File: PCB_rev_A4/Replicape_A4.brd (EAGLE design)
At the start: 100 x 69.6 mm, 191 parts, among them P8 F-2X23-, P9 F-2X23-, Q1 AON6758, Q2 AON6758, Q3 AON6758, Q4 NIF5002, Q5 NIF5002, Q6 NIF5002, U1 SN74AHC595PW, U10 RT8268, U11 PCA9685PW, U12 DAC088S085, U13 DRV8825PWP, U14 DRV8825PWP, U15 DRV8825PWP, U16 DRV8825PWP, U17 DRV8825PWP, U18 CAT24C256, U2 SN74AHC595PW, U3 SN74AHC595PW, U4 SN74AHC595PW, U5 SN74AHC595PW, U6 MCP16321, U7 MCP1402, U8 MCP1402, U9 MCP1402, X1 22-05-7028-02, X10 22-05-7028-02, X11 22-05-7028-02, X12 22-05-7038-03, X13 22-05-7028-02, X14 22-05-7048-04, X15 22-05-7048-04, X16 22-05-7048-04, X17 22-05-7048-04, X18 22-05-7048-04, X19 22-05-7028-02, X2 MSTBA4, X20 MSTBA4, X21 MSTBA2, X23 22-05-7028-02, X3 MSTBA2, X4 22-05-7028-02, X5 22-05-7028-02, X6 22-05-7028-02, X7 22-05-7038-03, X8 22-05-7038-03, X9 22-05-7038-03

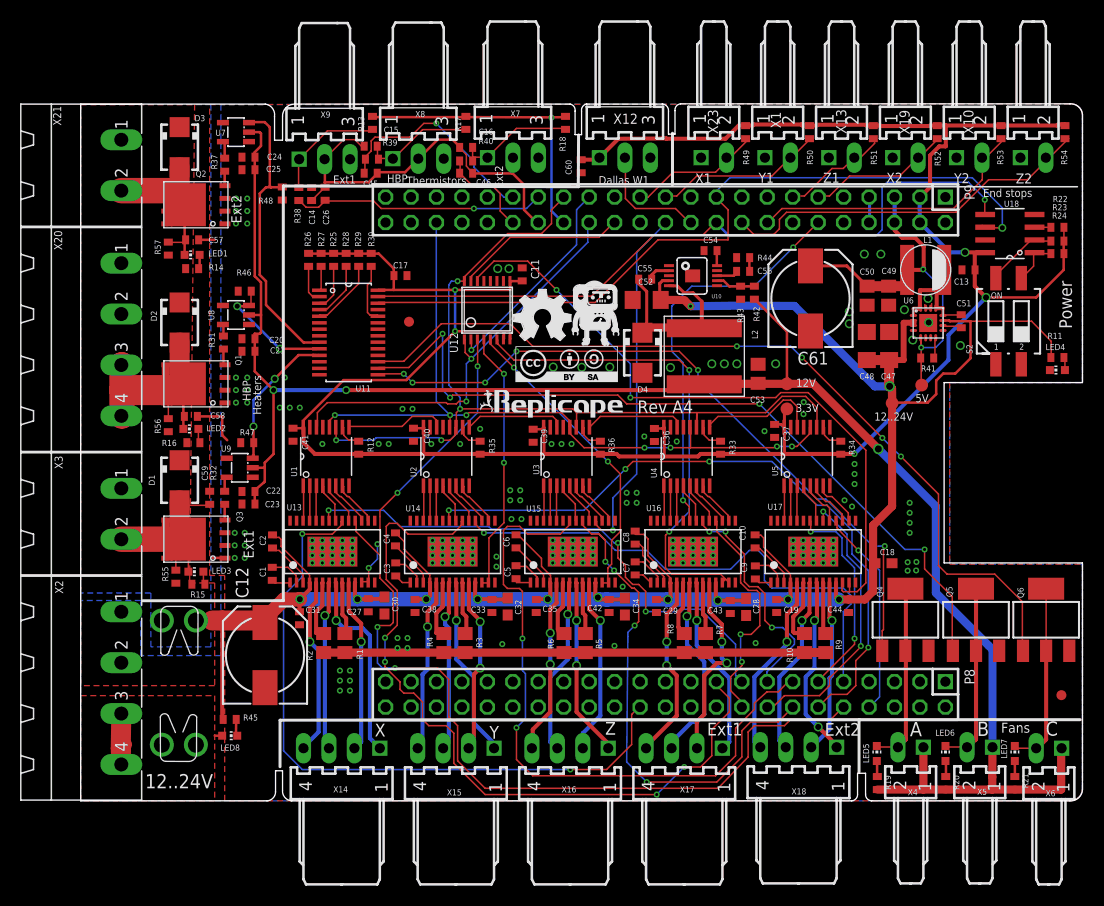
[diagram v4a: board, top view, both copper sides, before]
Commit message: Added a series resistor for Cboost to limit noise
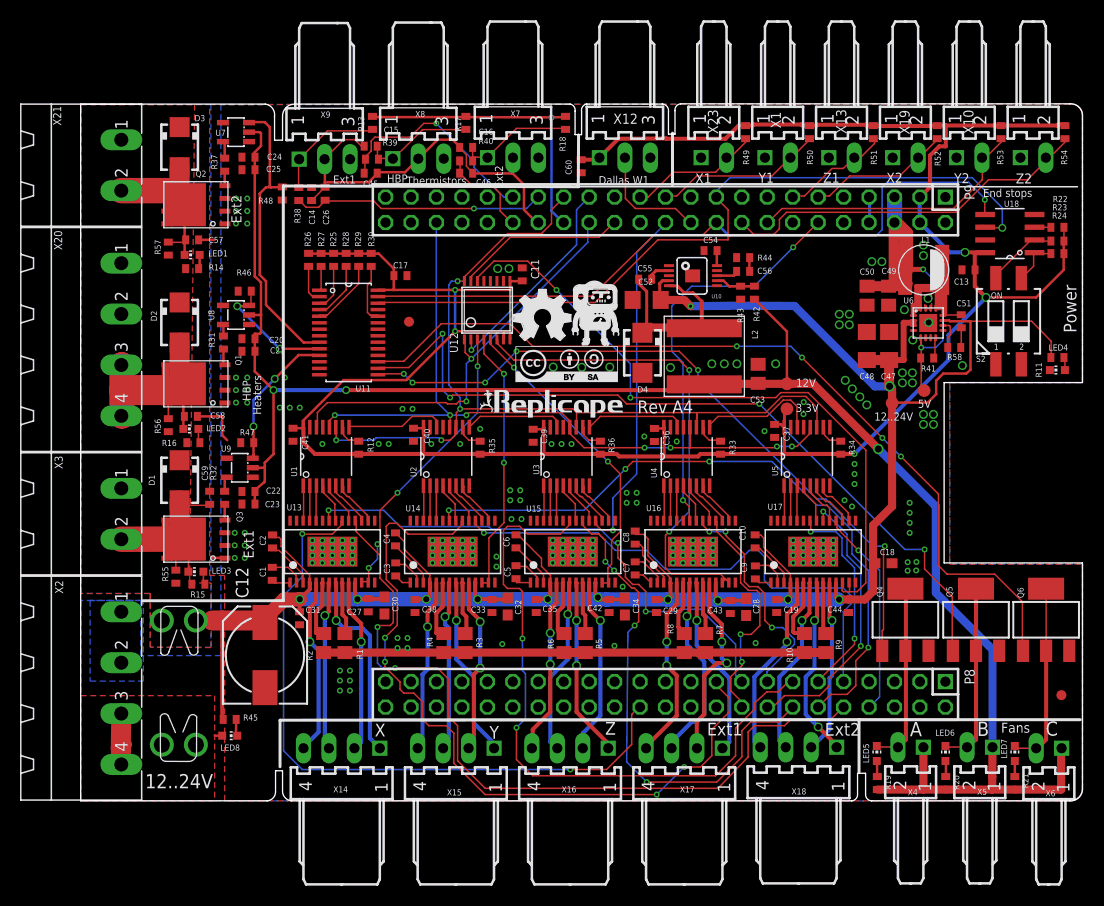
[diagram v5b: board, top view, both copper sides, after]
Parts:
- removed C61: 100uF, rcl:140CLH-0810
- added R58: 100R, rcl:R0402
- moved 5V 0.60 mm to (84.2, 41.0)
- moved L1 0.20 mm to (84.2, 53.0)
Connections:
- new net N$1: C51.1, R58.1
- net GND: no longer C61.-
- net N$128: now also R58.2; no longer C51.1
- net VDD_5V: no longer C61.+
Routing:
- net SW: track 12.7 -> 21.3 mm
- net VDD_IN: track 240.5 -> 242.8 mm
- net N$1: track 0.00 -> 1.98 mm
- net N$128: track 1.93 -> 3.08 mm
- net VDD_5V: track 40.1 -> 39.2 mm
- net GND: vias 196 -> 212
